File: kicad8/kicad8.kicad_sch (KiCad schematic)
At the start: 21 parts, among them J1 USB_C_Receptacle_USB2.0, U1 STM32F072CBT6, U2 PRTR5V0U2X

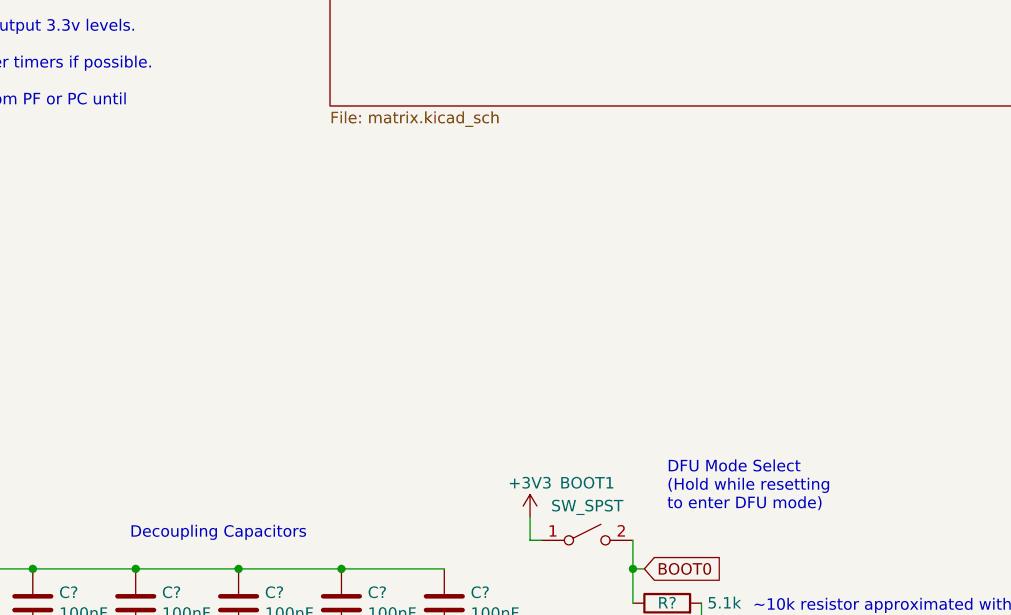
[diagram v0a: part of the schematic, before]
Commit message: Changed: switch footprint
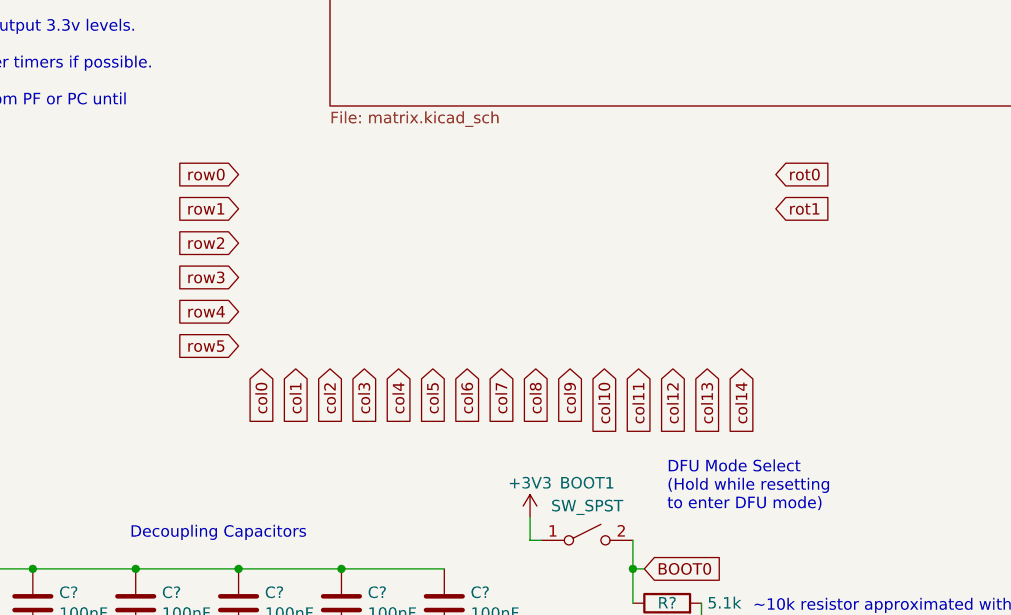
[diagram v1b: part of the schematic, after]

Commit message: Changed: Switch matrix layout
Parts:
- J1: footprint Connector_USB:USB_C_Receptacle_HRO_TYPE-C-31-M-12 -> PCM_marbastlib-various:USB_C_Receptacle_HRO_TYPE-C-31-M-12
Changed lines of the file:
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@@
 			)
 		)
-		(property "Footprint" "Connector_USB:USB_C_Receptacle_HRO_TYPE-C-31-M-12"
+		(property "Footprint" "PCM_marbastlib-various:USB_C_Receptacle_HRO_TYPE-C-31-M-12"
 			(at 36.83 151.765 0)
 			(effects

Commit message: Added: wiring to the switch matrix
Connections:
- net A10 is gone; now on net col0: U1.31 (PA10)
- net A14 is gone; now on net row2: U1.37 (PA14)
- net A15 is gone; now on net row1: U1.38 (PA15)
- net A4 is gone; now on net col14: U1.14 (PA4)
- net A5 is gone; now on net col13: U1.15 (PA5)
- net A6 is gone; now on net col12: U1.16 (PA6)
- net A7 is gone; now on net col11: U1.17 (PA7)
- net A8 is gone; now on net col2: U1.29 (PA8)
- net A9 is gone; now on net col1: U1.30 (PA9)
- net B0 is gone; now on net col10: U1.18 (PB0)
- net B1 is gone; now on net col9: U1.19 (PB1)
- net B10 is gone; now on net col7: U1.21 (PB10)
- net B12 is gone; now on net col6: U1.25 (PB12)
- net B13 is gone; now on net col5: U1.26 (PB13)
- net B14 is gone; now on net col4: U1.27 (PB14)
- net B15 is gone; now on net col3: U1.28 (PB15)
- net B2 is gone; now on net col8: U1.20 (PB2)
- net B3 is gone; now on net row0: U1.39 (PB3)
- net B5 is gone; now on net row5: U1.41 (PB5)
- net B6 is gone; now on net row4: U1.42 (PB6)
- net B7 is gone; now on net row3: U1.43 (PB7)

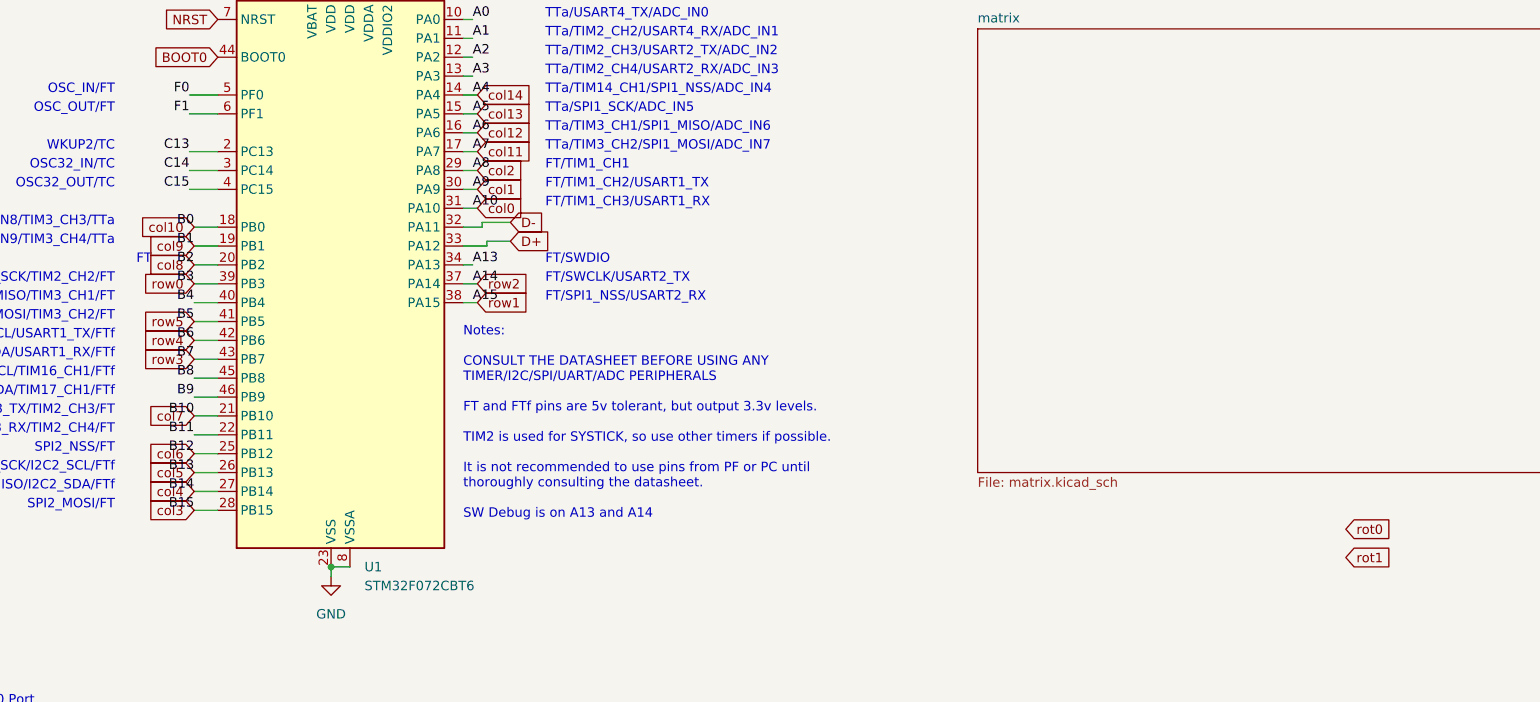
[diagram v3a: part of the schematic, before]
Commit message: Fixed: all clearance violations
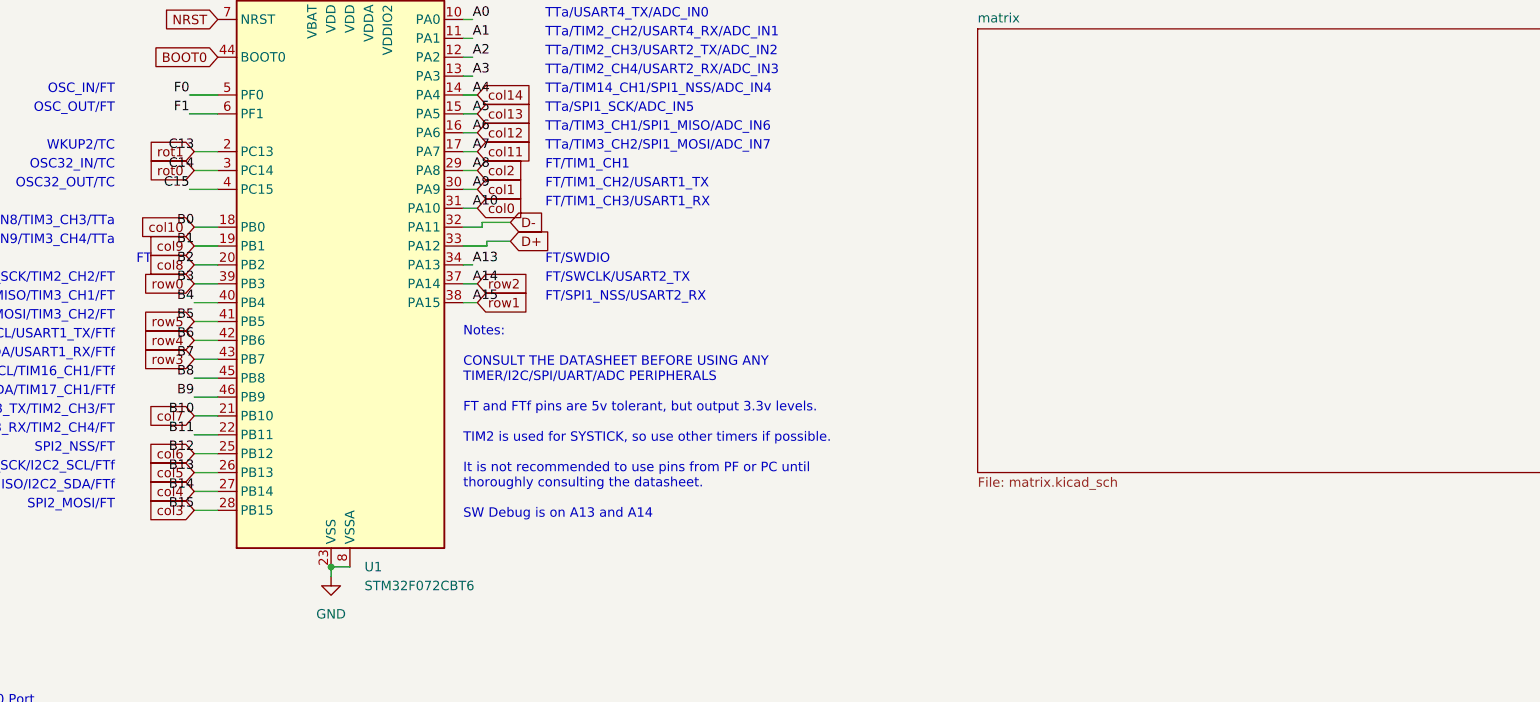
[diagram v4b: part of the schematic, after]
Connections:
- net C13 is gone; now on net rot1: U1.2 (PC13)
- net C14 is gone; now on net rot0: U1.3 (PC14)
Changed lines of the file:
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@@
+	(wire
+		(pts
+			(xy 60.96 48.26) (xy 64.135 48.26)
+		)
+		(stroke
+			(width 0)
+			(type default)
+		)
+	)
 	(wire
 		(pts
@@
 	(wire
 		(pts
-			(xy 60.325 48.26) (xy 64.135 48.26)
-		)
-		(stroke
-			(width 0)
-			(type default)
-		)
-	)
-	(wire
-		(pts
-			(xy 60.325 50.8) (xy 64.135 50.8)
+			(xy 60.96 50.8) (xy 64.135 50.8)
 		)
 		(stroke
@@
 	)
 	(label "C14"
-		(at 60.325 50.8 180)
+		(at 60.96 50.8 180)
 		(fields_autoplaced yes)
 		(effects
@@
 	)
 	(label "C13"
-		(at 60.325 48.26 180)
+		(at 60.96 48.26 180)
 		(fields_autoplaced yes)
 		(effects
@@
 	(global_label "rot1"
 		(shape input)
-		(at 215.9 102.87 0)
-		(fields_autoplaced yes)
-		(effects
-			(font
-				(size 1.27 1.27)
-			)
-			(justify left)
-		)
-		(property "Intersheetrefs" "${INTERSHEET_REFS}"
-			(at 222.7556 102.87 0)
-			(effects
-				(font
-					(size 1.27 1.27)
-				)
-				(justify left)
+		(at 60.96 48.26 180)
+		(fields_autoplaced yes)
+		(effects
+			(font
+				(size 1.27 1.27)
+			)
+			(justify right)
+		)
+		(property "Intersheetrefs" "${INTERSHEET_REFS}"
+			(at 54.1044 48.26 0)
+			(effects
+				(font
+					(size 1.27 1.27)
+				)
+				(justify right)
 				(hide yes)
 			)
@@
 	(global_label "rot0"
 		(shape input)
-		(at 215.9 99.06 0)
-		(fields_autoplaced yes)
-		(effects
-			(font
-				(size 1.27 1.27)
-			)
-			(justify left)
-		)
-		(property "Intersheetrefs" "${INTERSHEET_REFS}"
-			(at 222.7556 99.06 0)
-			(effects
-				(font
-					(size 1.27 1.27)
-				)
-				(justify left)
-				(hide yes)
-			)
+		(at 60.96 50.8 180)
+		(fields_autoplaced yes)
+		(effects
+			(font
+				(size 1.27 1.27)
+			)
+			(justify right)
+		)
+		(property "Intersheetrefs" "${INTERSHEET_REFS}"
+			(at 54.1044 50.8 0)
+			(effects
+				(font
+					(size 1.27 1.27)
+				)
+				(justify right)
+				(hide yes)
+			)

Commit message: -Added: Ground fill
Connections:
- net A0 is gone; now on net col13: U1.10 (PA0)
- net A1 is gone; now on net col11: U1.11 (PA1)
- net A2 is gone; now on net col10: U1.12 (PA2)
- net A3 is gone; now on net col9: U1.13 (PA3)
- net B11 is gone; now on net col0: U1.22 (PB11)
- net B4 is gone; now on net row1: U1.40 (PB4)
- net C15 is gone; now on net row3: U1.4 (PC15)
- net F0 is gone; now on net row4: U1.5 (PF0)
- net F1 is gone; now on net row5: U1.6 (PF1)
- net col0: no longer U1.31 (PA10)
- net col1: now also U1.21 (PB10); no longer U1.30 (PA9)
- net col10: no longer U1.18 (PB0)
- net col11: no longer U1.17 (PA7)
- net col12: now also U1.25 (PB12); no longer U1.16 (PA6)
- net col13: no longer U1.15 (PA5)
- net col14: now also U1.43 (PB7); no longer U1.14 (PA4)
- net col2: now also U1.20 (PB2); no longer U1.29 (PA8)
- net col3: now also U1.19 (PB1); no longer U1.28 (PB15)
- net col4: now also U1.18 (PB0); no longer U1.27 (PB14)
- net col5: now also U1.17 (PA7); no longer U1.26 (PB13)
- net col6: now also U1.16 (PA6); no longer U1.25 (PB12)
- net col7: now also U1.15 (PA5); no longer U1.21 (PB10)
- net col8: now also U1.14 (PA4); no longer U1.20 (PB2)
- net col9: no longer U1.19 (PB1)
- net rot0: now also U1.39 (PB3); no longer U1.3 (PC14)
- net rot1: now also U1.38 (PA15); no longer U1.2 (PC13)
- net row0: now also U1.37 (PA14); no longer U1.39 (PB3)
- net row1: no longer U1.38 (PA15)
- net row2: now also U1.3 (PC14); no longer U1.37 (PA14)
- net row3: no longer U1.43 (PB7)
- net row4: no longer U1.42 (PB6)
- net row5: no longer U1.41 (PB5)
- new net A10: U1.31 (PA10)
- new net A8: U1.29 (PA8)
- new net A9: U1.30 (PA9)
- new net B13: U1.26 (PB13)
- new net B14: U1.27 (PB14)
- new net B15: U1.28 (PB15)
- new net B5: U1.41 (PB5)
- new net B6: U1.42 (PB6)
- new net C13: U1.2 (PC13)
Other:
- added sheet RGB_Switch (RGB_Switch.kicad_sch)
- added sheet RGB_UL (RGB_UL.kicad_sch)

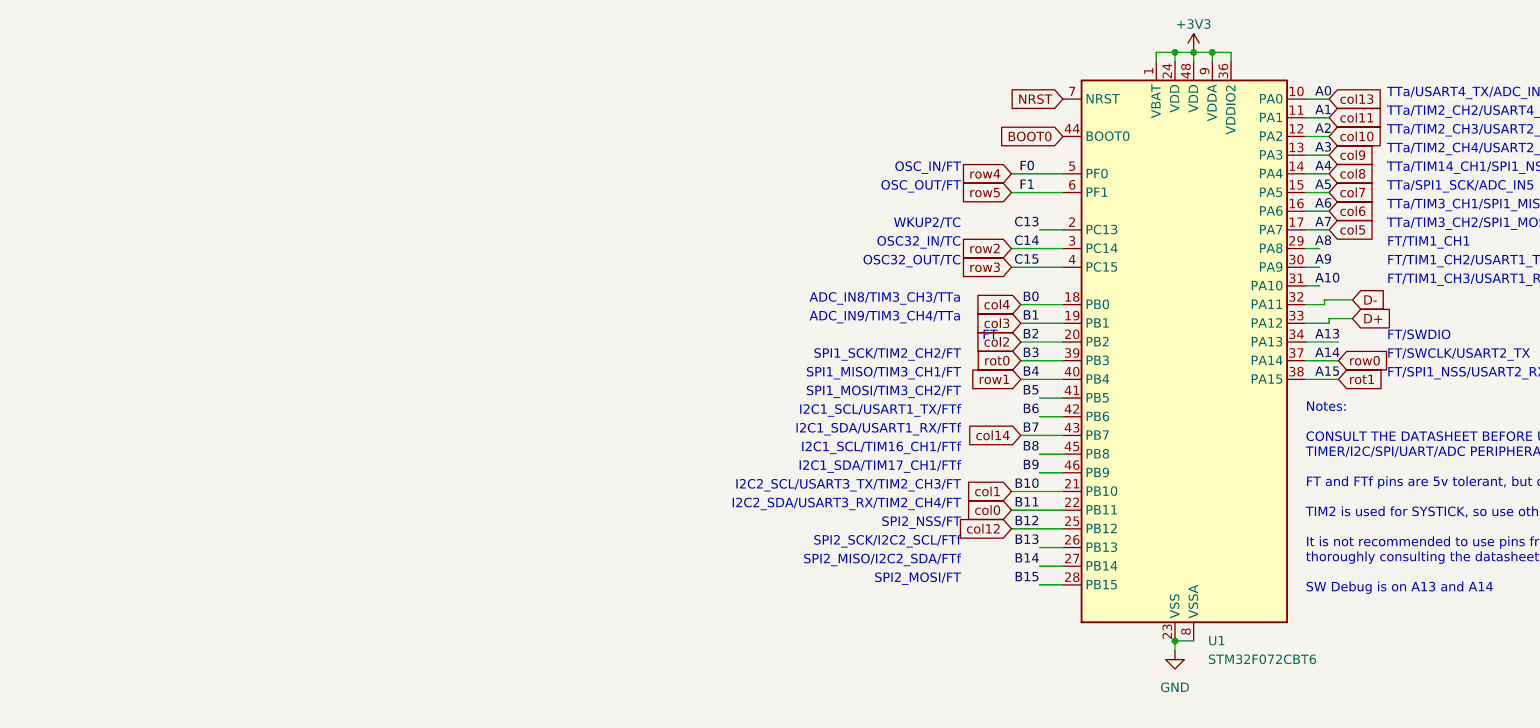
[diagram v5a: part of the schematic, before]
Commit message: Added: Stepped CAPS_LOCK and Split backspace
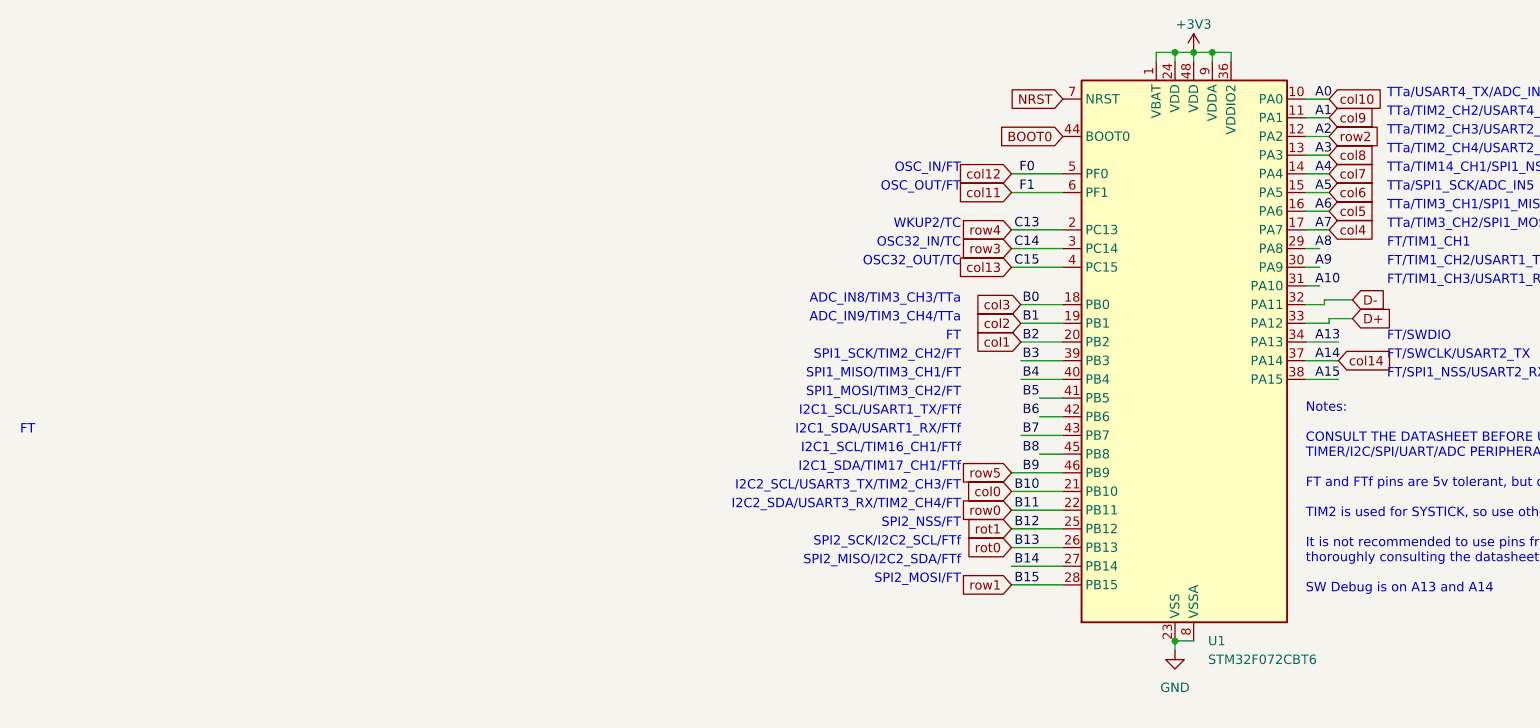
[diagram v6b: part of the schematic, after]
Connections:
- net B13 is gone; now on net rot0: U1.26 (PB13)
- net B15 is gone; now on net row1: U1.28 (PB15)
- net B9 is gone; now on net row5: U1.46 (PB9)
- net C13 is gone; now on net row4: U1.2 (PC13)
- net col0: now also U1.21 (PB10); no longer U1.22 (PB11)
- net col1: now also U1.20 (PB2); no longer U1.21 (PB10)
- net col10: now also U1.10 (PA0); no longer U1.12 (PA2)
- net col11: now also U1.6 (PF1); no longer U1.11 (PA1)
- net col12: now also U1.5 (PF0); no longer U1.25 (PB12)
- net col13: now also U1.4 (PC15); no longer U1.10 (PA0)
- net col14: now also U1.37 (PA14); no longer U1.43 (PB7)
- net col2: now also U1.19 (PB1); no longer U1.20 (PB2)
- net col3: now also U1.18 (PB0); no longer U1.19 (PB1)
- net col4: now also U1.17 (PA7); no longer U1.18 (PB0)
- net col5: now also U1.16 (PA6); no longer U1.17 (PA7)
- net col6: now also U1.15 (PA5); no longer U1.16 (PA6)
- net col7: now also U1.14 (PA4); no longer U1.15 (PA5)
- net col8: now also U1.13 (PA3); no longer U1.14 (PA4)
- net col9: now also U1.11 (PA1); no longer U1.13 (PA3)
- net rot0: no longer U1.39 (PB3)
- net rot1: now also U1.25 (PB12); no longer U1.38 (PA15)
- net row0: now also U1.22 (PB11); no longer U1.37 (PA14)
- net row1: no longer U1.40 (PB4)
- net row2: now also U1.12 (PA2); no longer U1.3 (PC14)
- net row3: now also U1.3 (PC14); no longer U1.4 (PC15)
- net row4: no longer U1.5 (PF0)
- net row5: no longer U1.6 (PF1)
- new net A15: U1.38 (PA15)
- new net B3: U1.39 (PB3)
- new net B4: U1.40 (PB4)
- new net B7: U1.43 (PB7)
